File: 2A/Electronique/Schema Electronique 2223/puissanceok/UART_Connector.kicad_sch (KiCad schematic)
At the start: 2 parts, among them J8 Conn_01x04

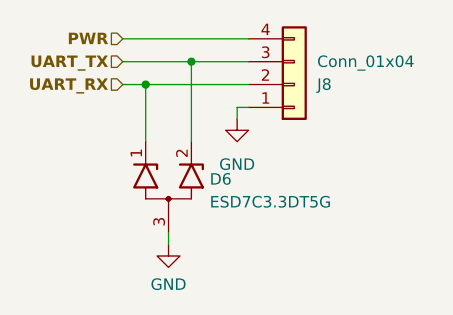
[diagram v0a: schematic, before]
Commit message: suppression diode et changement des feuille hiérarchique
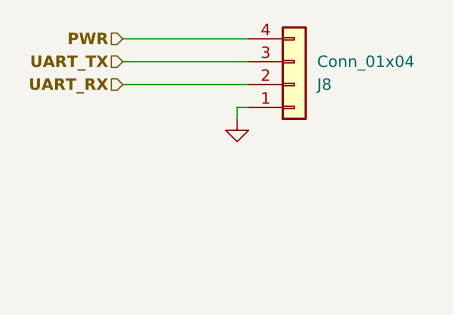
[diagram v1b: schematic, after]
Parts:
- removed D6: ESD7C3.3DT5G, Package_TO_SOT_SMD:SOT-416, symbol Power_Protection:RCLAMP0582B
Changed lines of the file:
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@@
 (kicad_sch (version 20230121) (generator eeschema)
   (paper "A4")
-  (junction (at 146.05 99.06) (diameter 0) (color 0 0 0 0)
-  )
-  (junction (at 140.97 101.6) (diameter 0) (color 0 0 0 0)
-  )
-  (wire (pts (xy 138.43 99.06) (xy 146.05 99.06))
-    (stroke (width 0) (type default))
-  )
-  (wire (pts (xy 138.43 101.6) (xy 140.97 101.6))
+  (wire (pts (xy 138.43 99.06) (xy 152.4 99.06))
     (stroke (width 0) (type default))
   )
   (wire (pts (xy 138.43 96.52) (xy 152.4 96.52))
-    (stroke (width 0) (type default))
-  )
-  (wire (pts (xy 143.51 119.38) (xy 143.51 118.11))
-    (stroke (width 0) (type default))
-  )
-  (wire (pts (xy 146.05 99.06) (xy 146.05 107.95))
     (stroke (width 0) (type default))
   )
@@
     (stroke (width 0) (type default))
   )
-  (wire (pts (xy 140.97 101.6) (xy 152.4 101.6))
-    (stroke (width 0) (type default))
-  )
-  (wire (pts (xy 140.97 101.6) (xy 140.97 107.95))
-    (stroke (width 0) (type default))
-  )
-  (wire (pts (xy 146.05 99.06) (xy 152.4 99.06))
+  (wire (pts (xy 138.43 101.6) (xy 152.4 101.6))
     (stroke (width 0) (type default))
   )
@@
     (effects (font (size 1.27 1.27) bold) (justify right))
   )
-  (symbol (lib_id "power:GND") (at 143.51 119.38 0) (unit 1)
-    (in_bom yes) (on_board yes) (dnp no) (fields_autoplaced)
-    (property "Reference" "#PWR015" (at 143.51 125.73 0)
-      (effects (font (size 1.27 1.27)) hide)
-    )
-    (property "Value" "GND" (at 143.51 123.8234 0)
-      (effects (font (size 1.27 1.27)))
-    )
-    (property "Footprint" "" (at 143.51 119.38 0)
-      (effects (font (size 1.27 1.27)) hide)
-    )
-    (property "Datasheet" "" (at 143.51 119.38 0)
-      (effects (font (size 1.27 1.27)) hide)
-    )
-    (pin "1")
-    (instances
-      (project "puissanceok"
-        (path "/50648b18-b1a7-4d76-a5dd-1fad5f3e825e/af50aa95-aed2-4d54-9537-cfc75f526261"
-          (reference "#PWR015") (unit 1)
-        )
-        (path "/50648b18-b1a7-4d76-a5dd-1fad5f3e825e/87662431-78a9-4c9d-bc49-d5c8947794ed"
-          (reference "#PWR037") (unit 1)
-        )
-        (path "/50648b18-b1a7-4d76-a5dd-1fad5f3e825e/78b7270a-a5a1-4fe9-b966-10927640cfad"
-          (reference "#PWR038") (unit 1)
-        )
-      )
-    )
-  )
-  (symbol (lib_id "Power_Protection:RCLAMP0582B") (at 143.51 113.03 90) (unit 1)
-    (in_bom yes) (on_board yes) (dnp no) (fields_autoplaced)
-    (property "Reference" "D6" (at 148.082 112.1318 90)
-      (effects (font (size 1.27 1.27)) (justify right))
-    )
-    (property "Value" "ESD7C3.3DT5G" (at 148.082 114.6687 90)
-      (effects (font (size 1.27 1.27)) (justify right))
-    )
-    (property "Footprint" "Package_TO_SOT_SMD:SOT-416" (at 151.13 113.03 0)
-      (effects (font (size 1.27 1.27)) hide)
-    )
-    (property "Datasheet" "https://www.mouser.fr/datasheet/2/308/1/ESD7C3_3D_D-2311593.pdf" (at 140.97 111.76 0)
-      (effects (font (size 1.27 1.27)) hide)
-    )
-    (property "Mouser Part Number" "863-ESD7C5.0DT5G" (at 143.51 113.03 90)
-      (effects (font (size 1.27 1.27)) hide)
-    )
-    (pin "3")
-    (pin "1")
-    (pin "2")
-    (instances
-      (project "puissanceok"
-        (path "/50648b18-b1a7-4d76-a5dd-1fad5f3e825e/af50aa95-aed2-4d54-9537-cfc75f526261"
-          (reference "D6") (unit 1)
-        )
-        (path "/50648b18-b1a7-4d76-a5dd-1fad5f3e825e/87662431-78a9-4c9d-bc49-d5c8947794ed"
-          (reference "D7") (unit 1)
-        )
-        (path "/50648b18-b1a7-4d76-a5dd-1fad5f3e825e/78b7270a-a5a1-4fe9-b966-10927640cfad"
-          (reference "D8") (unit 1)
-        )
-      )
-    )
-  )
   (symbol (lib_id "power:GND") (at 151.13 105.41 0) (unit 1)
     (in_bom yes) (on_board yes) (dnp no) (fields_autoplaced)
@@
     )
     (property "Value" "GND" (at 151.13 110.49 0)
-      (effects (font (size 1.27 1.27)))
+      (effects (font (size 1.27 1.27)) hide)
     )
     (property "Footprint" "" (at 151.13 105.41 0)

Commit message: update schematic
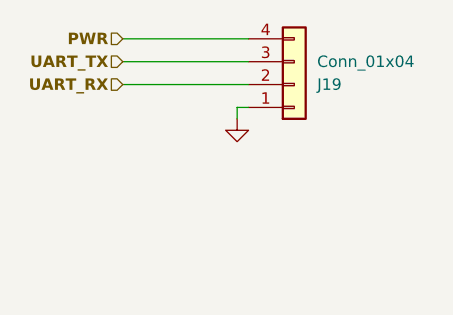
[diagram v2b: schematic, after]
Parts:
- renumbered J8 to J19
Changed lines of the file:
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@@
   (symbol (lib_id "power:GND") (at 151.13 105.41 0) (unit 1)
     (in_bom yes) (on_board yes) (dnp no) (fields_autoplaced)
-    (property "Reference" "#PWR017" (at 151.13 111.76 0)
+    (property "Reference" "#PWR049" (at 151.13 111.76 0)
       (effects (font (size 1.27 1.27)) hide)
     )
@@
       (project "puissanceok"
         (path "/50648b18-b1a7-4d76-a5dd-1fad5f3e825e/87662431-78a9-4c9d-bc49-d5c8947794ed"
-          (reference "#PWR017") (unit 1)
+          (reference "#PWR049") (unit 1)
         )
         (path "/50648b18-b1a7-4d76-a5dd-1fad5f3e825e/af50aa95-aed2-4d54-9537-cfc75f526261"
-          (reference "#PWR017") (unit 1)
+          (reference "#PWR044") (unit 1)
         )
         (path "/50648b18-b1a7-4d76-a5dd-1fad5f3e825e/78b7270a-a5a1-4fe9-b966-10927640cfad"
-          (reference "#PWR017") (unit 1)
+          (reference "#PWR050") (unit 1)
         )
       )
@@
   (symbol (lib_id "Connector_Generic:Conn_01x04") (at 157.48 101.6 0) (mirror x) (unit 1)
     (in_bom yes) (on_board yes) (dnp no)
-    (property "Reference" "J8" (at 160.02 101.6 0)
+    (property "Reference" "J19" (at 160.02 101.6 0)
       (effects (font (size 1.27 1.27)) (justify left))
     )
@@
       (project "puissanceok"
         (path "/50648b18-b1a7-4d76-a5dd-1fad5f3e825e/87662431-78a9-4c9d-bc49-d5c8947794ed"
-          (reference "J8") (unit 1)
+          (reference "J19") (unit 1)
         )
         (path "/50648b18-b1a7-4d76-a5dd-1fad5f3e825e/78b7270a-a5a1-4fe9-b966-10927640cfad"
-          (reference "J8") (unit 1)
+          (reference "J20") (unit 1)
         )
         (path "/50648b18-b1a7-4d76-a5dd-1fad5f3e825e/af50aa95-aed2-4d54-9537-cfc75f526261"
-          (reference "J8") (unit 1)
+          (reference "J17") (unit 1)
         )
       )

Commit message: update pcd
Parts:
- J22: renamed from J19; footprint (none) -> Connector_JST:JST_XH_B4B-XH-A_1x04_P2.50mm_Vertical
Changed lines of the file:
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@@
   (symbol (lib_id "power:GND") (at 151.13 105.41 0) (unit 1)
     (in_bom yes) (on_board yes) (dnp no) (fields_autoplaced)
-    (property "Reference" "#PWR049" (at 151.13 111.76 0)
+    (property "Reference" "#PWR051" (at 151.13 111.76 0)
       (effects (font (size 1.27 1.27)) hide)
     )
@@
       (project "puissanceok"
         (path "/50648b18-b1a7-4d76-a5dd-1fad5f3e825e/87662431-78a9-4c9d-bc49-d5c8947794ed"
-          (reference "#PWR049") (unit 1)
+          (reference "#PWR051") (unit 1)
         )
         (path "/50648b18-b1a7-4d76-a5dd-1fad5f3e825e/af50aa95-aed2-4d54-9537-cfc75f526261"
-          (reference "#PWR044") (unit 1)
+          (reference "#PWR046") (unit 1)
         )
         (path "/50648b18-b1a7-4d76-a5dd-1fad5f3e825e/78b7270a-a5a1-4fe9-b966-10927640cfad"
-          (reference "#PWR050") (unit 1)
+          (reference "#PWR052") (unit 1)
         )
       )
@@
   (symbol (lib_id "Connector_Generic:Conn_01x04") (at 157.48 101.6 0) (mirror x) (unit 1)
     (in_bom yes) (on_board yes) (dnp no)
-    (property "Reference" "J19" (at 160.02 101.6 0)
+    (property "Reference" "J22" (at 160.02 101.6 0)
       (effects (font (size 1.27 1.27)) (justify left))
     )
@@
       (effects (font (size 1.27 1.27)) (justify left))
     )
-    (property "Footprint" "" (at 157.48 101.6 0)
+    (property "Footprint" "Connector_JST:JST_XH_B4B-XH-A_1x04_P2.50mm_Vertical" (at 157.48 101.6 0)
       (effects (font (size 1.27 1.27)) hide)
     )
@@
       (project "puissanceok"
         (path "/50648b18-b1a7-4d76-a5dd-1fad5f3e825e/87662431-78a9-4c9d-bc49-d5c8947794ed"
-          (reference "J19") (unit 1)
+          (reference "J22") (unit 1)
         )
         (path "/50648b18-b1a7-4d76-a5dd-1fad5f3e825e/78b7270a-a5a1-4fe9-b966-10927640cfad"
+          (reference "J23") (unit 1)
+        )
+        (path "/50648b18-b1a7-4d76-a5dd-1fad5f3e825e/af50aa95-aed2-4d54-9537-cfc75f526261"
           (reference "J20") (unit 1)
         )
-        (path "/50648b18-b1a7-4d76-a5dd-1fad5f3e825e/af50aa95-aed2-4d54-9537-cfc75f526261"
-          (reference "J17") (unit 1)
-        )
       )

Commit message: finalize schematic + footprints
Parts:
- J22: value Conn_01x04 -> Conn_UART
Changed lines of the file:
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@@
       (effects (font (size 1.27 1.27)) (justify left))
     )
-    (property "Value" "Conn_01x04" (at 160.02 99.06 0)
+    (property "Value" "Conn_UART" (at 160.02 99.06 0)
       (effects (font (size 1.27 1.27)) (justify left))
     )

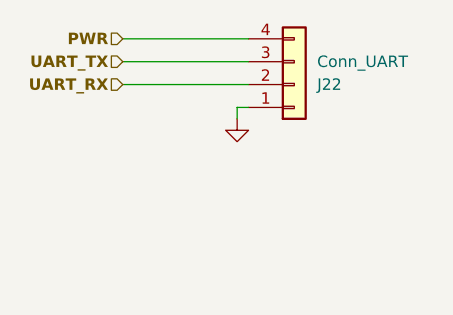
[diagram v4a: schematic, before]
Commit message: pcb place components and add power/gnd planes
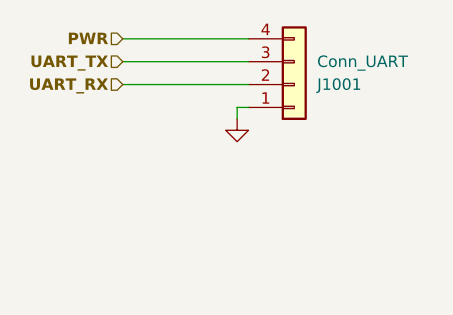
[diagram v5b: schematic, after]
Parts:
- renumbered J22 to J1001
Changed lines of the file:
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@@
   (symbol (lib_id "power:GND") (at 151.13 105.41 0) (unit 1)
     (in_bom yes) (on_board yes) (dnp no) (fields_autoplaced)
-    (property "Reference" "#PWR051" (at 151.13 111.76 0)
+    (property "Reference" "#PWR01001" (at 151.13 111.76 0)
       (effects (font (size 1.27 1.27)) hide)
     )
@@
       (project "puissanceok"
         (path "/50648b18-b1a7-4d76-a5dd-1fad5f3e825e/87662431-78a9-4c9d-bc49-d5c8947794ed"
-          (reference "#PWR051") (unit 1)
+          (reference "#PWR01001") (unit 1)
         )
         (path "/50648b18-b1a7-4d76-a5dd-1fad5f3e825e/af50aa95-aed2-4d54-9537-cfc75f526261"
-          (reference "#PWR046") (unit 1)
+          (reference "#PWR0801") (unit 1)
         )
         (path "/50648b18-b1a7-4d76-a5dd-1fad5f3e825e/78b7270a-a5a1-4fe9-b966-10927640cfad"
-          (reference "#PWR052") (unit 1)
+          (reference "#PWR01101") (unit 1)
         )
       )
@@
   (symbol (lib_id "Connector_Generic:Conn_01x04") (at 157.48 101.6 0) (mirror x) (unit 1)
     (in_bom yes) (on_board yes) (dnp no)
-    (property "Reference" "J22" (at 160.02 101.6 0)
+    (property "Reference" "J1001" (at 160.02 101.6 0)
       (effects (font (size 1.27 1.27)) (justify left))
     )
@@
       (project "puissanceok"
         (path "/50648b18-b1a7-4d76-a5dd-1fad5f3e825e/87662431-78a9-4c9d-bc49-d5c8947794ed"
-          (reference "J22") (unit 1)
+          (reference "J1001") (unit 1)
         )
         (path "/50648b18-b1a7-4d76-a5dd-1fad5f3e825e/78b7270a-a5a1-4fe9-b966-10927640cfad"
-          (reference "J23") (unit 1)
+          (reference "J1101") (unit 1)
         )
         (path "/50648b18-b1a7-4d76-a5dd-1fad5f3e825e/af50aa95-aed2-4d54-9537-cfc75f526261"
-          (reference "J20") (unit 1)
+          (reference "J801") (unit 1)
         )
       )
